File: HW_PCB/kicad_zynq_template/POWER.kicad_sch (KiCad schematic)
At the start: 9 parts, among them U7 EN5311QI, U8 EN5311QI

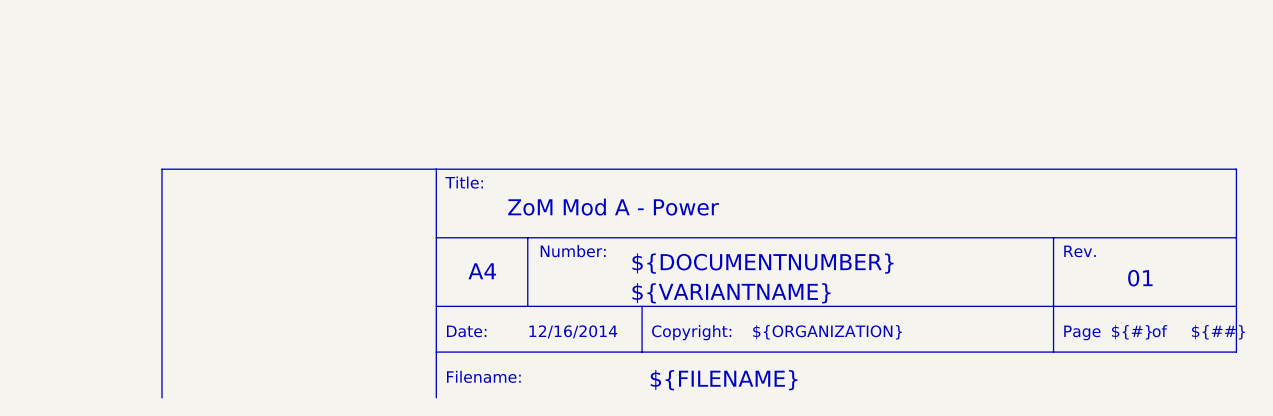
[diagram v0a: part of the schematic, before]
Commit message: pcbs tidied up
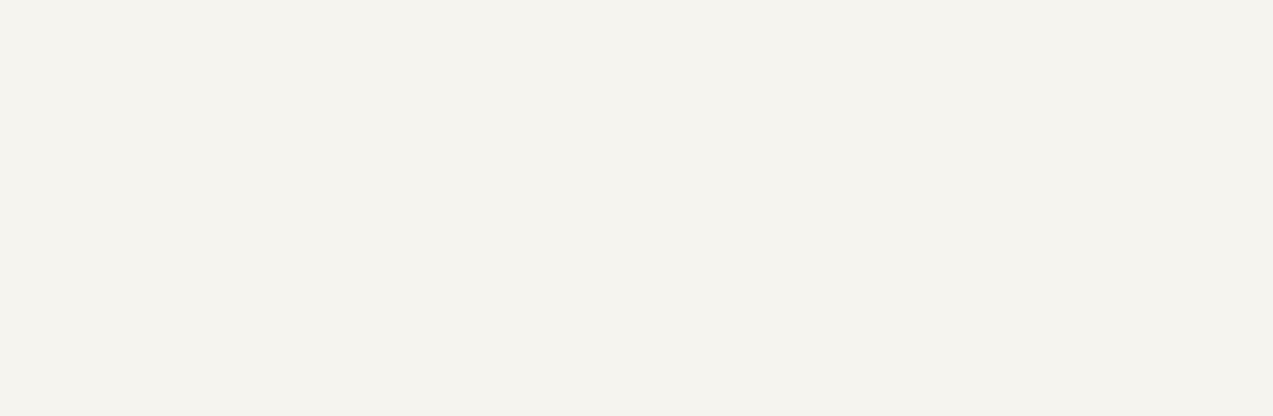
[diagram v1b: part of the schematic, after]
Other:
- note removed: "${##}"
- note removed: "${#}"
- note removed: "${DOCUMENTNUMBER}"
- note removed: "${FILENAME}"
- note removed: "${ISSUE_DATE}"
- note removed: "${ORGANIZATION}"
- note removed: "${REVISION}"
- note removed: "${TITLE}"
- note removed: "${VARIANTNAME}"
- note removed: "A4"
- note removed: "Copyright:"
- note removed: "Date:"
- note removed: "Filename:"
- note removed: "Number:"
- note removed: "Page"
- note removed: "Rev."
- note removed: "Title:"
- note removed: "of"
